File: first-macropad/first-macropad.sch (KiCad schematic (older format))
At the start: 9 parts

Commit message: step 5 done
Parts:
- added C? (x2): 22pF, symbol Device:C_Small
- added R?: 10k, symbol Device:R_Small
- added SW?: SW_Push, symbol Switch:SW_Push
- added Y?: 16MHz, symbol Device:Crystal_GND24_Small
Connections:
- net labels added: D+, D-
- wire segments 25 -> 46
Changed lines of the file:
@@
 Wire Wire Line
 	4500 3100 4050 3100
-Wire Wire Line
-	3850 3100 3200 3100
-Wire Wire Line
-	3400 3200 3200 3200
 $Comp
 L Device:C_Small C?
@@
 Wire Wire Line
 	4050 2900 4500 2900
+$Comp
+L Device:Crystal_GND24_Small Y?
+U 1 1 66FCAFBC
+P 3600 2400
+F 0 "Y?" V 3554 2544 50  0000 L CNN
+F 1 "16MHz" V 3645 2544 50  0000 L CNN
+F 2 "" H 3600 2400 50  0001 C CNN
+F 3 "~" H 3600 2400 50  0001 C CNN
+	1    3600 2400
+	0    1    1    0
+$EndComp
+$Comp
+L Device:C_Small C?
+U 1 1 66FCDD8A
+P 3300 2550
+F 0 "C?" V 3071 2550 50  0000 C CNN
+F 1 "22pF" V 3162 2550 50  0000 C CNN
+F 2 "" H 3300 2550 50  0001 C CNN
+F 3 "~" H 3300 2550 50  0001 C CNN
+	1    3300 2550
+	0    1    1    0
+$EndComp
+$Comp
+L power:GND #PWR?
+U 1 1 66FCE651
+P 3200 2750
+F 0 "#PWR?" H 3200 2500 50  0001 C CNN
+F 1 "GND" H 3205 2577 50  0000 C CNN
+F 2 "" H 3200 2750 50  0001 C CNN
+F 3 "" H 3200 2750 50  0001 C CNN
+	1    3200 2750
+	1    0    0    -1
+$EndComp
+Connection ~ 3200 2550
+Wire Wire Line
+	3200 2550 3200 2750
+Wire Wire Line
+	3400 2550 3400 2500
+Wire Wire Line
+	3400 2500 3600 2500
+Connection ~ 3600 2500
+Wire Wire Line
+	3400 2300 3600 2300
+Connection ~ 3600 2300
+Wire Wire Line
+	3700 2400 3700 2650
+Wire Wire Line
+	3700 2650 3500 2650
+Wire Wire Line
+	3450 2650 3450 2750
+Wire Wire Line
+	3450 2750 3200 2750
+Wire Wire Line
+	3500 2400 3500 2650
+Connection ~ 3500 2650
+Wire Wire Line
+	3500 2650 3450 2650
+Wire Wire Line
+	3400 2150 3400 2300
+Wire Wire Line
+	3200 2150 3200 2550
+$Comp
+L Device:C_Small C?
+U 1 1 66FCD691
+P 3300 2150
+F 0 "C?" V 3071 2150 50  0000 C CNN
+F 1 "22pF" V 3162 2150 50  0000 C CNN
+F 2 "" H 3300 2150 50  0001 C CNN
+F 3 "~" H 3300 2150 50  0001 C CNN
+	1    3300 2150
+	0    1    1    0
+$EndComp
+$Comp
+L Switch:SW_Push SW?
+U 1 1 66FD6AA1
+P 4150 2100
+F 0 "SW?" H 4150 2385 50  0000 C CNN
+F 1 "SW_Push" H 4150 2294 50  0000 C CNN
+F 2 "" H 4150 2300 50  0001 C CNN
+F 3 "~" H 4150 2300 50  0001 C CNN
+	1    4150 2100
+	1    0    0    -1
+$EndComp
+Wire Wire Line
+	4350 2100 4400 2100
+Wire Wire Line
+	3950 2100 3950 1850
+$Comp
+L power:GND #PWR?
+U 1 1 66FD9ABF
+P 3750 1950
+F 0 "#PWR?" H 3750 1700 50  0001 C CNN
+F 1 "GND" H 3755 1777 50  0000 C CNN
+F 2 "" H 3750 1950 50  0001 C CNN
+F 3 "" H 3750 1950 50  0001 C CNN
+	1    3750 1950
+	1    0    0    -1
+$EndComp
+$Comp
+L Device:R_Small R?
+U 1 1 66FDA140
+P 4400 1650
+F 0 "R?" H 4459 1696 50  0000 L CNN
+F 1 "10k" H 4459 1605 50  0000 L CNN
+F 2 "" H 4400 1650 50  0001 C CNN
+F 3 "~" H 4400 1650 50  0001 C CNN
+	1    4400 1650
+	1    0    0    -1
+$EndComp
+$Comp
+L power:+5V #PWR?
+U 1 1 66FDAF28
+P 4400 1450
+F 0 "#PWR?" H 4400 1300 50  0001 C CNN
+F 1 "+5V" H 4415 1623 50  0000 C CNN
+F 2 "" H 4400 1450 50  0001 C CNN
+F 3 "" H 4400 1450 50  0001 C CNN
+	1    4400 1450
+	1    0    0    -1
+$EndComp
+Wire Wire Line
+	4400 1450 4400 1550
+Wire Wire Line
+	4400 1750 4400 2100
+Connection ~ 4400 2100
+Wire Wire Line
+	4400 2100 4500 2100
+Text GLabel 2900 3100 0    50   Input ~ 0
+D+
+Text GLabel 2900 3200 0    50   Input ~ 0
+D-
+Connection ~ 3200 2750
+Wire Wire Line
+	3600 2300 4500 2300
+Wire Wire Line
+	3600 2500 4500 2500
+Wire Wire Line
+	3750 1950 3750 1850
+Wire Wire Line
+	3750 1850 3950 1850
+Wire Wire Line
+	2900 3200 3400 3200
+Wire Wire Line
+	2900 3100 3850 3100
 $EndSCHEMATC

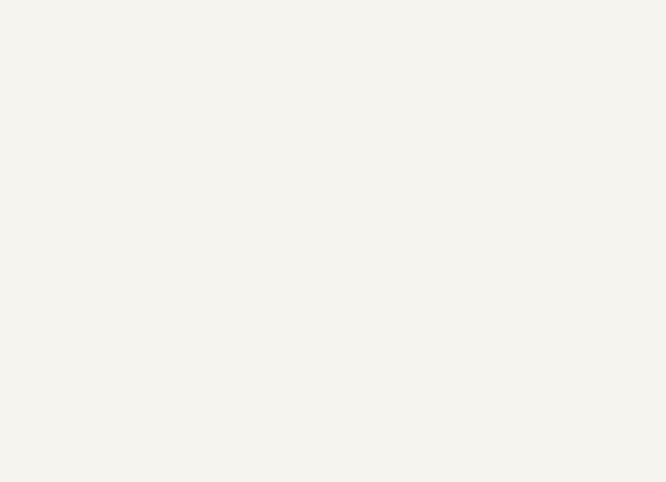
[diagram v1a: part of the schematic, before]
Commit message: up to after the mcu for ai03 guide
honestly going to reset this and look into the kiCad file for xiao 2040
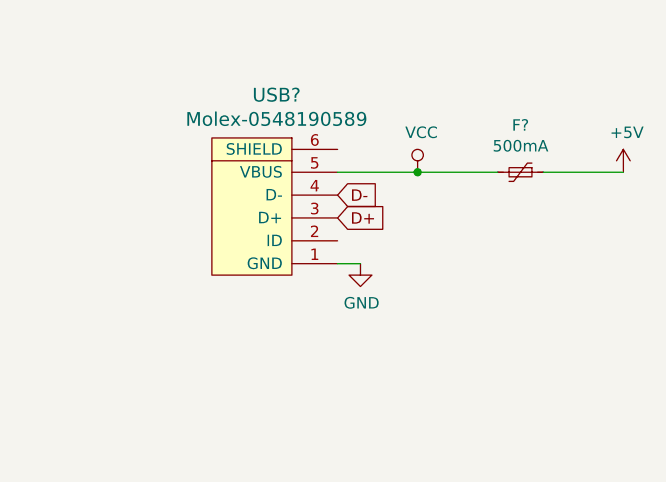
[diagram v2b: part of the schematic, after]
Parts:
- added F?: 500mA, symbol Device:Polyfuse_Small
- added USB?: Molex-0548190589, symbol random-keyboard-parts:Molex-0548190589
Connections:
- net +5V: now also F?.1
- net D+: now also USB?.3 (D+)
- net D-: now also USB?.4 (D-)
- net GND: now also USB?.1 (GND)
- new net VCC: F?.2, USB?.5 (VBUS)
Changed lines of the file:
@@
 Wire Wire Line
 	2900 3100 3850 3100
+$Comp
+L random-keyboard-parts:Molex-0548190589 USB?
+U 1 1 66FF0933
+P 7900 2100
+F 0 "USB?" V 8437 2067 60  0000 C CNN
+F 1 "Molex-0548190589" V 8331 2067 60  0000 C CNN
+F 2 "" H 7900 2100 60  0001 C CNN
+F 3 "" H 7900 2100 60  0001 C CNN
+	1    7900 2100
+	0    -1   -1   0
+$EndComp
+$Comp
+L Device:Polyfuse_Small F?
+U 1 1 66FF3ADA
+P 9000 1900
+F 0 "F?" V 8795 1900 50  0000 C CNN
+F 1 "500mA" V 8886 1900 50  0000 C CNN
+F 2 "" H 9050 1700 50  0001 L CNN
+F 3 "~" H 9000 1900 50  0001 C CNN
+	1    9000 1900
+	0    1    1    0
+$EndComp
+Wire Wire Line
+	8200 1900 8550 1900
+$Comp
+L power:+5V #PWR?
+U 1 1 66FF9B9C
+P 9450 1900
+F 0 "#PWR?" H 9450 1750 50  0001 C CNN
+F 1 "+5V" H 9465 2073 50  0000 C CNN
+F 2 "" H 9450 1900 50  0001 C CNN
+F 3 "" H 9450 1900 50  0001 C CNN
+	1    9450 1900
+	1    0    0    -1
+$EndComp
+Wire Wire Line
+	9100 1900 9450 1900
+$Comp
+L power:VCC #PWR?
+U 1 1 66FFC50C
+P 8550 1900
+F 0 "#PWR?" H 8550 1750 50  0001 C CNN
+F 1 "VCC" H 8567 2073 50  0000 C CNN
+F 2 "" H 8550 1900 50  0001 C CNN
+F 3 "" H 8550 1900 50  0001 C CNN
+	1    8550 1900
+	1    0    0    -1
+$EndComp
+Connection ~ 8550 1900
+Wire Wire Line
+	8550 1900 8900 1900
+Text GLabel 8200 2000 2    50   Input ~ 0
+D-
+Text GLabel 8200 2100 2    50   Input ~ 0
+D+
+$Comp
+L power:GND #PWR?
+U 1 1 66FFEE97
+P 8300 2300
+F 0 "#PWR?" H 8300 2050 50  0001 C CNN
+F 1 "GND" H 8305 2127 50  0000 C CNN
+F 2 "" H 8300 2300 50  0001 C CNN
+F 3 "" H 8300 2300 50  0001 C CNN
+	1    8300 2300
+	1    0    0    -1
+$EndComp
+Wire Wire Line
+	8200 2300 8300 2300
 $EndSCHEMATC
